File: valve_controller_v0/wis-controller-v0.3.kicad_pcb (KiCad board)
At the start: 2 copper layers, 78 x 110 mm, 68 parts, among them J1 18650 Socket, J11 Solenoid_connector, J3 USB_C_Receptacle_USB2.0, J5 SWD, J6 JST-2PH, Q1 DMG3415UQ-7, SW1 RESET, SW3 SW_DIP_x02, SW4 BOOT, U1 RAK3172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

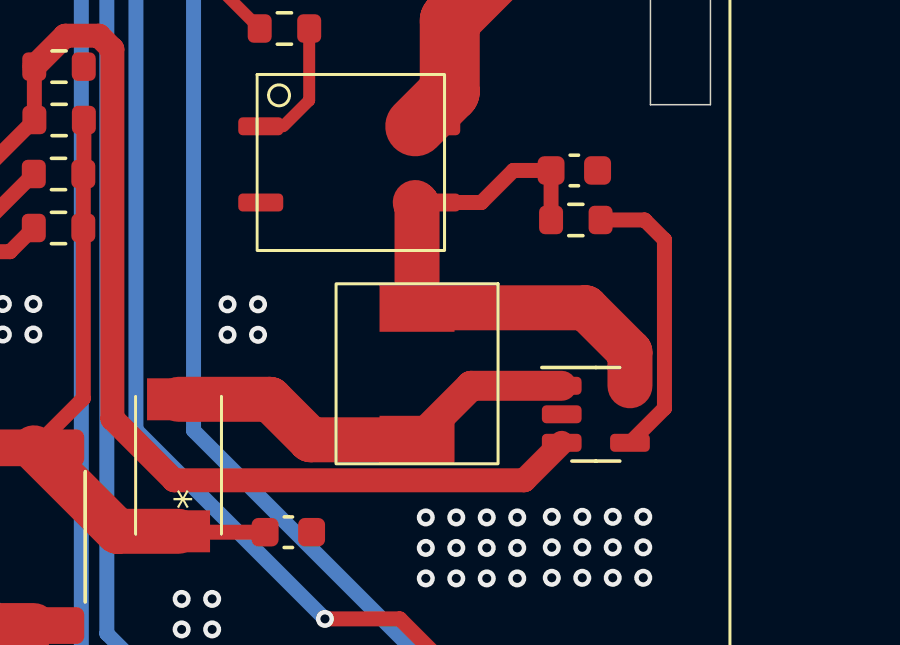
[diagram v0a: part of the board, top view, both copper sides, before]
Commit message: Corrected inductor L2 footprint
The footprint of L2 was incorrect and JLCPCB rejected to solder it (The same design was already manufactured before)
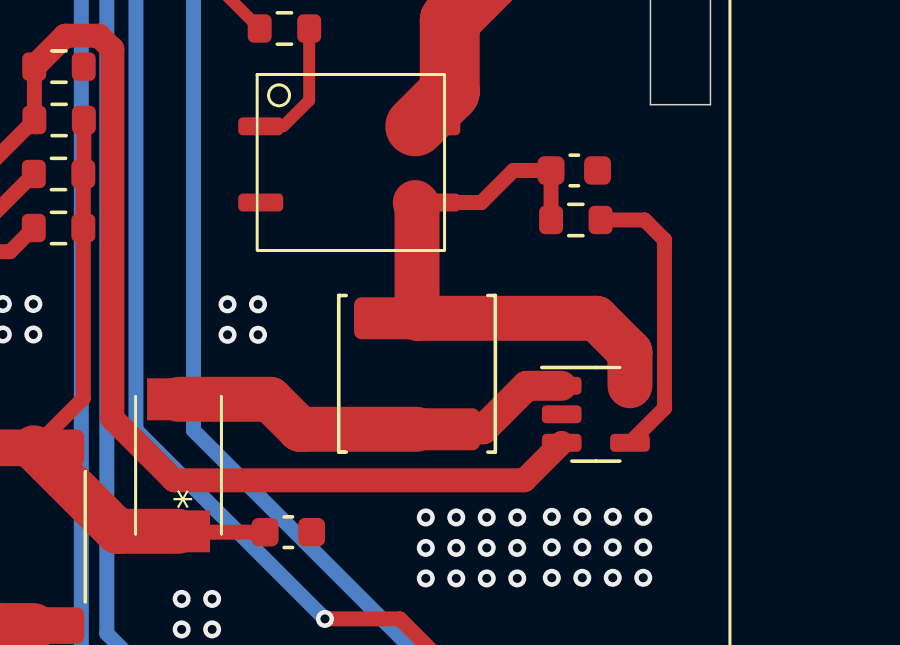
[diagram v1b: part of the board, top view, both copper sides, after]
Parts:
- L2: footprint WIS_Solenoid_Power_module:Inductor_6R8 -> Inductor_SMD:L_Changjiang_FNR5040S
